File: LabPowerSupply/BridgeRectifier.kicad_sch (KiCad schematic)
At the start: 9 parts

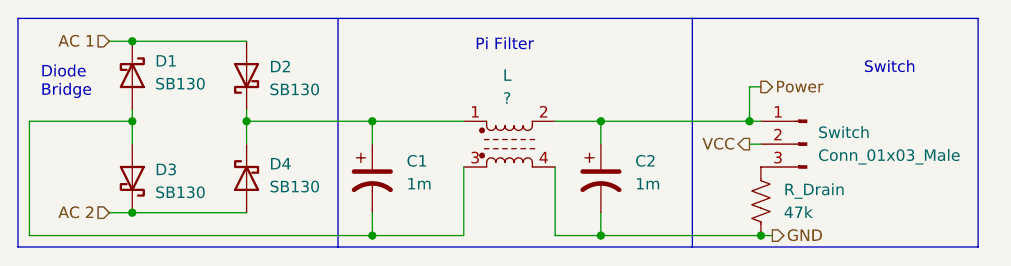
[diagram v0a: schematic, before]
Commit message: Finished first pass on the schematic
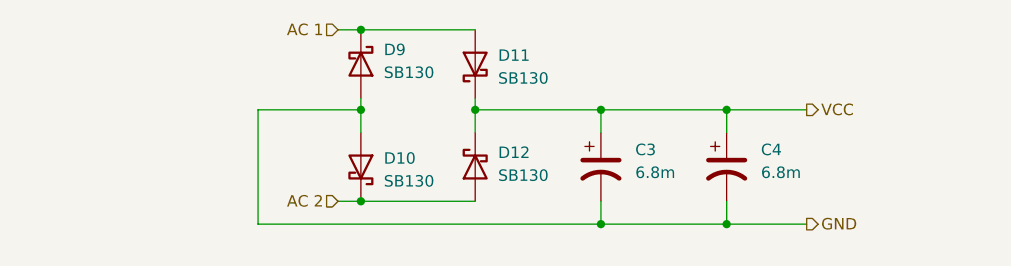
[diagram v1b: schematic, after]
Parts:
- removed C2: 1m, Capacitor_THT:CP_Radial_D13.0mm_P5.00mm, symbol Device:C_Polarized_US
- removed L: ?, Inductor_SMD:L_Bourns_SRF1260, symbol Device:L_Ferrite_Coupled
- removed R_Drain: 47k, Resistor_SMD:R_1210_3225Metric, symbol Device:R_US
- removed Switch: Conn_01x03_Male, Connector_JST:JST_VH_B3P-VH-B_1x03_P3.96mm_Vertical, symbol Connector:Conn_01x03_Male
- added C4: 6.8m, Capacitor_THT:CP_Radial_D18.0mm_P7.50mm, symbol Device:C_Polarized_US
- C3: renamed from C1; value 1m -> 6.8m; footprint Capacitor_THT:CP_Radial_D13.0mm_P5.00mm -> Capacitor_THT:CP_Radial_D18.0mm_P7.50mm
- renumbered D3 to D10, D2 to D11, D4 to D12, D1 to D9
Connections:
- net GND: now also C3.2, D10.2 (A), D9.2 (A), C4.2
- net VCC: now also C3.1, D11.1 (K), D12.1 (K), C4.1
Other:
- note removed: "Diode Bridge"
- note removed: "Pi Filter"
- note removed: "Switch"
- moved on the sheet: C3, D10, D11, D12, D9

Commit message: more work
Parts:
- renumbered C3 to C1_BR1, C4 to C2_BR1, D9 to D1_BR1, D11 to D2_BR1, D10 to D3_BR1, D12 to D4_BR1
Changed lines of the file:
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@@
     (rev "2")
     (company "George Mason University")
+    (comment 2 "smooth out the ripple to give a constant DC voltage.")
+    (comment 3 "transformer into a DC voltage. Two 6.8mF capacitiors are used to")
+    (comment 4 "The bridge rectifier is used to turn the AC output of the")
   )
   (junction (at 143.51 95.25) (diameter 0) (color 0 0 0 0)
@@
   (symbol (lib_id "Device:C_Polarized_US") (at 171.45 101.6 0) (unit 1)
     (in_bom yes) (on_board yes) (fields_autoplaced)
-    (property "Reference" "C4" (id 0) (at 175.26 99.6949 0)
+    (property "Reference" "C2_BR1" (id 0) (at 175.26 99.6949 0)
       (effects (font (size 1.27 1.27)) (justify left))
     )
@@
   (symbol (lib_id "Device:C_Polarized_US") (at 157.48 101.6 0) (unit 1)
     (in_bom yes) (on_board yes) (fields_autoplaced)
-    (property "Reference" "C3" (id 0) (at 161.29 99.6949 0)
+    (property "Reference" "C1_BR1" (id 0) (at 161.29 99.6949 0)
       (effects (font (size 1.27 1.27)) (justify left))
     )
@@
   (symbol (lib_id "Diode:SB130") (at 130.81 101.6 270) (mirror x) (unit 1)
     (in_bom yes) (on_board yes) (fields_autoplaced)
-    (property "Reference" "D10" (id 0) (at 133.35 100.6474 90)
+    (property "Reference" "D3_BR1" (id 0) (at 133.35 100.6474 90)
       (effects (font (size 1.27 1.27)) (justify left))
     )
@@
   (symbol (lib_id "Diode:SB130") (at 143.51 90.17 90) (unit 1)
     (in_bom yes) (on_board yes) (fields_autoplaced)
-    (property "Reference" "D11" (id 0) (at 146.05 89.2174 90)
+    (property "Reference" "D2_BR1" (id 0) (at 146.05 89.2174 90)
       (effects (font (size 1.27 1.27)) (justify right))
     )
@@
   (symbol (lib_id "Diode:SB130") (at 130.81 90.17 270) (unit 1)
     (in_bom yes) (on_board yes) (fields_autoplaced)
-    (property "Reference" "D9" (id 0) (at 133.35 88.5824 90)
+    (property "Reference" "D1_BR1" (id 0) (at 133.35 88.5824 90)
       (effects (font (size 1.27 1.27)) (justify left))
     )
@@
   (symbol (lib_id "Diode:SB130") (at 143.51 101.6 90) (mirror x) (unit 1)
     (in_bom yes) (on_board yes) (fields_autoplaced)
-    (property "Reference" "D12" (id 0) (at 146.05 100.0124 90)
+    (property "Reference" "D4_BR1" (id 0) (at 146.05 100.0124 90)
       (effects (font (size 1.27 1.27)) (justify right))
     )

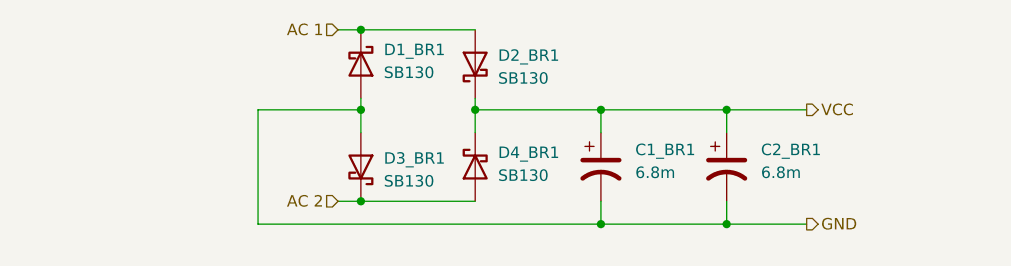
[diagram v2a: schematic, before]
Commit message: Resistor footprints changed to 0603
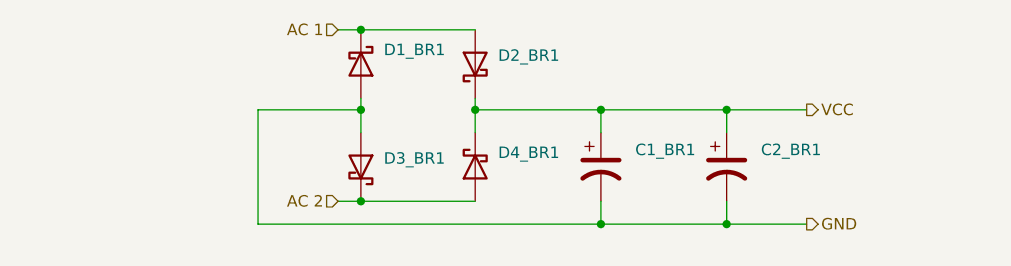
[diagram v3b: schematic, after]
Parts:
- C1_BR1, C2_BR1: value 6.8m -> (none); footprint Capacitor_THT:CP_Radial_D18.0mm_P7.50mm -> (none)
- D1_BR1, D2_BR1, D3_BR1, D4_BR1: value SB130 -> (none); footprint Diode_THT:D_DO-41_SOD81_P10.16mm_Horizontal -> (none)
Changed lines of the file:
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@@
       (effects (font (size 1.27 1.27)) (justify left))
     )
-    (property "Value" "6.8m" (id 1) (at 175.26 102.2349 0)
+    (property "Value" "" (id 1) (at 175.26 102.2349 0)
       (effects (font (size 1.27 1.27)) (justify left))
     )
-    (property "Footprint" "Capacitor_THT:CP_Radial_D18.0mm_P7.50mm" (id 2) (at 171.45 101.6 0)
+    (property "Footprint" "" (id 2) (at 171.45 101.6 0)
       (effects (font (size 1.27 1.27)) hide)
     )
@@
       (effects (font (size 1.27 1.27)) (justify left))
     )
-    (property "Value" "6.8m" (id 1) (at 161.29 102.2349 0)
+    (property "Value" "" (id 1) (at 161.29 102.2349 0)
       (effects (font (size 1.27 1.27)) (justify left))
     )
-    (property "Footprint" "Capacitor_THT:CP_Radial_D18.0mm_P7.50mm" (id 2) (at 157.48 101.6 0)
+    (property "Footprint" "" (id 2) (at 157.48 101.6 0)
       (effects (font (size 1.27 1.27)) hide)
     )
@@
       (effects (font (size 1.27 1.27)) (justify left))
     )
-    (property "Value" "SB130" (id 1) (at 133.35 103.1874 90)
+    (property "Value" "" (id 1) (at 133.35 103.1874 90)
       (effects (font (size 1.27 1.27)) (justify left))
     )
-    (property "Footprint" "Diode_THT:D_DO-41_SOD81_P10.16mm_Horizontal" (id 2) (at 126.365 101.6 0)
+    (property "Footprint" "" (id 2) (at 126.365 101.6 0)
       (effects (font (size 1.27 1.27)) hide)
     )
@@
       (effects (font (size 1.27 1.27)) (justify right))
     )
-    (property "Value" "SB130" (id 1) (at 146.05 91.7574 90)
+    (property "Value" "" (id 1) (at 146.05 91.7574 90)
       (effects (font (size 1.27 1.27)) (justify right))
     )
-    (property "Footprint" "Diode_THT:D_DO-41_SOD81_P10.16mm_Horizontal" (id 2) (at 147.955 90.17 0)
+    (property "Footprint" "" (id 2) (at 147.955 90.17 0)
       (effects (font (size 1.27 1.27)) hide)
     )
@@
       (effects (font (size 1.27 1.27)) (justify left))
     )
-    (property "Value" "SB130" (id 1) (at 133.35 91.1224 90)
+    (property "Value" "" (id 1) (at 133.35 91.1224 90)
       (effects (font (size 1.27 1.27)) (justify left))
     )
-    (property "Footprint" "Diode_THT:D_DO-41_SOD81_P10.16mm_Horizontal" (id 2) (at 126.365 90.17 0)
+    (property "Footprint" "" (id 2) (at 126.365 90.17 0)
       (effects (font (size 1.27 1.27)) hide)
     )
@@
       (effects (font (size 1.27 1.27)) (justify right))
     )
-    (property "Value" "SB130" (id 1) (at 146.05 102.5524 90)
+    (property "Value" "" (id 1) (at 146.05 102.5524 90)
       (effects (font (size 1.27 1.27)) (justify right))
     )
-    (property "Footprint" "Diode_THT:D_DO-41_SOD81_P10.16mm_Horizontal" (id 2) (at 147.955 101.6 0)
+    (property "Footprint" "" (id 2) (at 147.955 101.6 0)
       (effects (font (size 1.27 1.27)) hide)
     )

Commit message: Added mcu capacitors, split 5v inductors
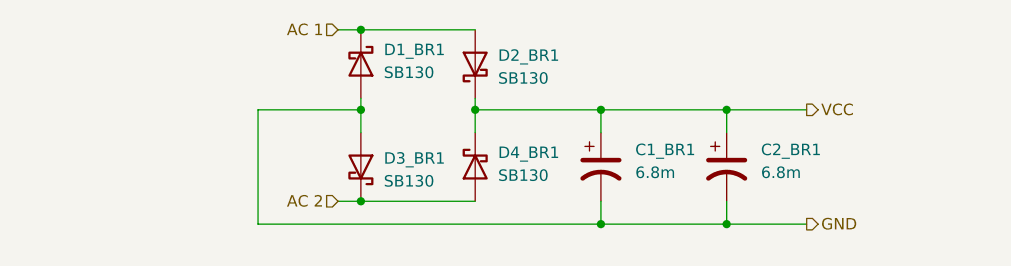
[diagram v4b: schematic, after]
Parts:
- C1_BR1, C2_BR1: value (none) -> 6.8m; footprint (none) -> Capacitor_THT:CP_Radial_D18.0mm_P7.50mm
- D1_BR1, D2_BR1, D3_BR1, D4_BR1: value (none) -> SB130; footprint (none) -> Diode_THT:D_DO-41_SOD81_P10.16mm_Horizontal
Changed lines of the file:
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@@
       (effects (font (size 1.27 1.27)) (justify left))
     )
-    (property "Value" "" (id 1) (at 175.26 102.2349 0)
+    (property "Value" "6.8m" (id 1) (at 175.26 102.2349 0)
       (effects (font (size 1.27 1.27)) (justify left))
     )
-    (property "Footprint" "" (id 2) (at 171.45 101.6 0)
+    (property "Footprint" "Capacitor_THT:CP_Radial_D18.0mm_P7.50mm" (id 2) (at 171.45 101.6 0)
       (effects (font (size 1.27 1.27)) hide)
     )
@@
       (effects (font (size 1.27 1.27)) (justify left))
     )
-    (property "Value" "" (id 1) (at 161.29 102.2349 0)
+    (property "Value" "6.8m" (id 1) (at 161.29 102.2349 0)
       (effects (font (size 1.27 1.27)) (justify left))
     )
-    (property "Footprint" "" (id 2) (at 157.48 101.6 0)
+    (property "Footprint" "Capacitor_THT:CP_Radial_D18.0mm_P7.50mm" (id 2) (at 157.48 101.6 0)
       (effects (font (size 1.27 1.27)) hide)
     )
@@
       (effects (font (size 1.27 1.27)) (justify left))
     )
-    (property "Value" "" (id 1) (at 133.35 103.1874 90)
+    (property "Value" "SB130" (id 1) (at 133.35 103.1874 90)
       (effects (font (size 1.27 1.27)) (justify left))
     )
-    (property "Footprint" "" (id 2) (at 126.365 101.6 0)
+    (property "Footprint" "Diode_THT:D_DO-41_SOD81_P10.16mm_Horizontal" (id 2) (at 126.365 101.6 0)
       (effects (font (size 1.27 1.27)) hide)
     )
@@
       (effects (font (size 1.27 1.27)) (justify right))
     )
-    (property "Value" "" (id 1) (at 146.05 91.7574 90)
+    (property "Value" "SB130" (id 1) (at 146.05 91.7574 90)
       (effects (font (size 1.27 1.27)) (justify right))
     )
-    (property "Footprint" "" (id 2) (at 147.955 90.17 0)
+    (property "Footprint" "Diode_THT:D_DO-41_SOD81_P10.16mm_Horizontal" (id 2) (at 147.955 90.17 0)
       (effects (font (size 1.27 1.27)) hide)
     )
@@
       (effects (font (size 1.27 1.27)) (justify left))
     )
-    (property "Value" "" (id 1) (at 133.35 91.1224 90)
+    (property "Value" "SB130" (id 1) (at 133.35 91.1224 90)
       (effects (font (size 1.27 1.27)) (justify left))
     )
-    (property "Footprint" "" (id 2) (at 126.365 90.17 0)
+    (property "Footprint" "Diode_THT:D_DO-41_SOD81_P10.16mm_Horizontal" (id 2) (at 126.365 90.17 0)
       (effects (font (size 1.27 1.27)) hide)
     )
@@
       (effects (font (size 1.27 1.27)) (justify right))
     )
-    (property "Value" "" (id 1) (at 146.05 102.5524 90)
+    (property "Value" "SB130" (id 1) (at 146.05 102.5524 90)
       (effects (font (size 1.27 1.27)) (justify right))
     )
-    (property "Footprint" "" (id 2) (at 147.955 101.6 0)
+    (property "Footprint" "Diode_THT:D_DO-41_SOD81_P10.16mm_Horizontal" (id 2) (at 147.955 101.6 0)
       (effects (font (size 1.27 1.27)) hide)
     )

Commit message: Changed most parts to smd
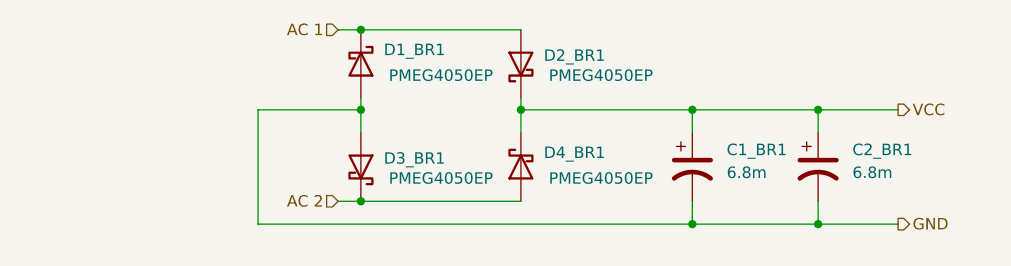
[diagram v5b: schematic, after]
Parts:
- D1_BR1, D2_BR1, D3_BR1, D4_BR1: value SB130 -> PMEG4050EP; footprint Diode_THT:D_DO-41_SOD81_P10.16mm_Horizontal -> Diode_SMD:D_SOD-128; symbol Diode:SB130 -> Diode:PMEG4050EP
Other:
- moved on the sheet: C1_BR1, C2_BR1, D2_BR1, D4_BR1

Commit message: Updated Part List
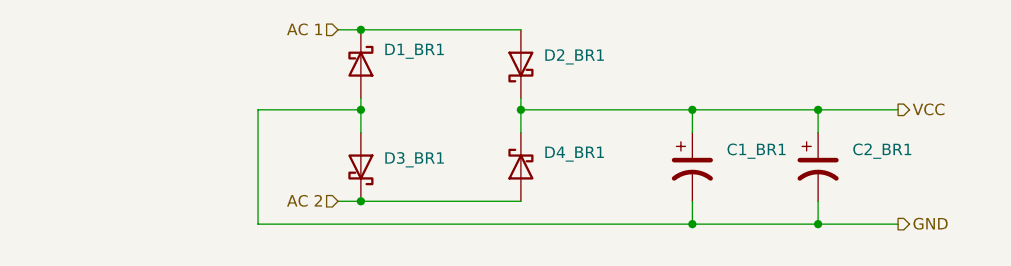
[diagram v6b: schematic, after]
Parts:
- C1_BR1, C2_BR1: value 6.8m -> (none); footprint Capacitor_THT:CP_Radial_D18.0mm_P7.50mm -> (none)
- D1_BR1, D2_BR1, D3_BR1, D4_BR1: value PMEG4050EP -> (none); footprint Diode_SMD:D_SOD-128 -> (none)
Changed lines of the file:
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@@
       (effects (font (size 1.27 1.27)) (justify left))
     )
-    (property "Value" "6.8m" (id 1) (at 185.42 102.2349 0)
+    (property "Value" "" (id 1) (at 185.42 102.2349 0)
       (effects (font (size 1.27 1.27)) (justify left))
     )
-    (property "Footprint" "Capacitor_THT:CP_Radial_D18.0mm_P7.50mm" (id 2) (at 181.61 101.6 0)
+    (property "Footprint" "" (id 2) (at 181.61 101.6 0)
       (effects (font (size 1.27 1.27)) hide)
     )
@@
       (effects (font (size 1.27 1.27)) (justify left))
     )
-    (property "Value" "6.8m" (id 1) (at 171.45 102.2349 0)
+    (property "Value" "" (id 1) (at 171.45 102.2349 0)
       (effects (font (size 1.27 1.27)) (justify left))
     )
-    (property "Footprint" "Capacitor_THT:CP_Radial_D18.0mm_P7.50mm" (id 2) (at 167.64 101.6 0)
+    (property "Footprint" "" (id 2) (at 167.64 101.6 0)
       (effects (font (size 1.27 1.27)) hide)
     )
@@
       (effects (font (size 1.27 1.27)) (justify left))
     )
-    (property "Value" "PMEG4050EP" (id 1) (at 139.7 102.87 90))
-    (property "Footprint" "Diode_SMD:D_SOD-128" (id 2) (at 126.365 101.6 0)
+    (property "Value" "" (id 1) (at 139.7 102.87 90))
+    (property "Footprint" "" (id 2) (at 126.365 101.6 0)
       (effects (font (size 1.27 1.27)) hide)
     )
@@
       (effects (font (size 1.27 1.27)) (justify right))
     )
-    (property "Value" "PMEG4050EP" (id 1) (at 157.48 91.44 90))
-    (property "Footprint" "Diode_SMD:D_SOD-128" (id 2) (at 153.035 90.17 0)
+    (property "Value" "" (id 1) (at 157.48 91.44 90))
+    (property "Footprint" "" (id 2) (at 153.035 90.17 0)
       (effects (font (size 1.27 1.27)) hide)
     )
@@
       (effects (font (size 1.27 1.27)) (justify left))
     )
-    (property "Value" "PMEG4050EP" (id 1) (at 139.7 91.44 90))
-    (property "Footprint" "Diode_SMD:D_SOD-128" (id 2) (at 126.365 90.17 0)
+    (property "Value" "" (id 1) (at 139.7 91.44 90))
+    (property "Footprint" "" (id 2) (at 126.365 90.17 0)
       (effects (font (size 1.27 1.27)) hide)
     )
@@
       (effects (font (size 1.27 1.27)) (justify right))
     )
-    (property "Value" "PMEG4050EP" (id 1) (at 157.48 102.87 90))
-    (property "Footprint" "Diode_SMD:D_SOD-128" (id 2) (at 153.035 101.6 0)
+    (property "Value" "" (id 1) (at 157.48 102.87 90))
+    (property "Footprint" "" (id 2) (at 153.035 101.6 0)
       (effects (font (size 1.27 1.27)) hide)
     )
